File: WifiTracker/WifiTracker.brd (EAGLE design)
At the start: 80 x 44.1 mm, 23 parts, among them Y1 16MHz

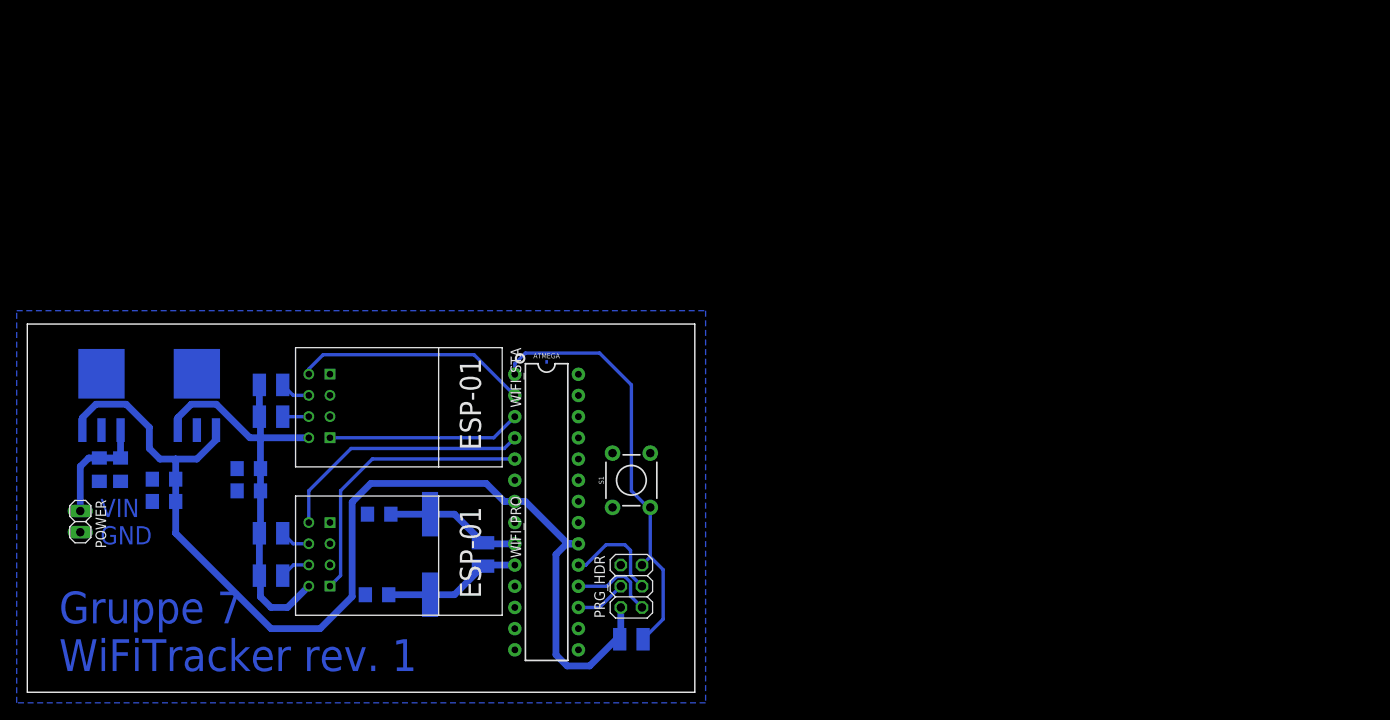
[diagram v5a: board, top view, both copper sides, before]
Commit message: Added 5v to 3.3V regulators to Wifitrackers
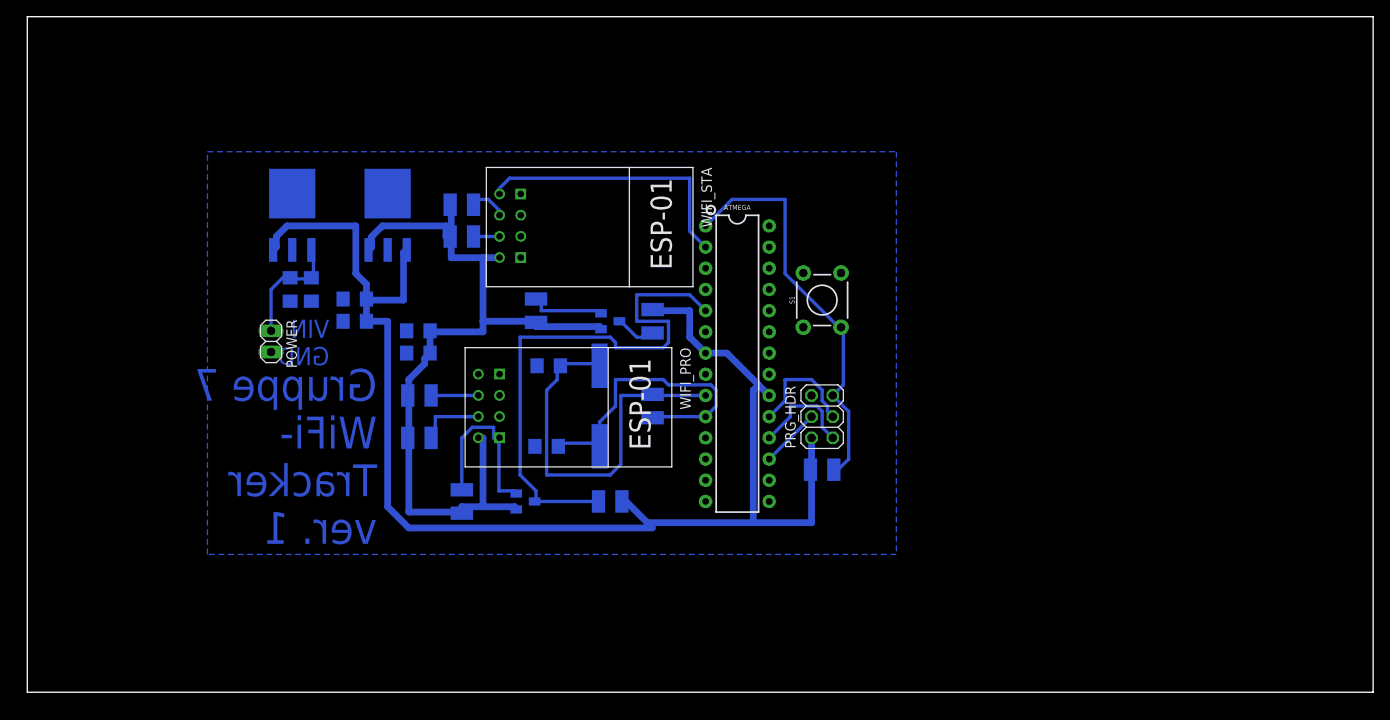
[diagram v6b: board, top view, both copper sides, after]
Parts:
- added Q1, Q2: BSS123, transistor-small-signal:SOT23
- added R10, R7, R8, R9: 10kΩ, eagle-ltspice:R1210
- R1, R2: value 10KOHM -> 10KΩ
- R3, R5, R6: value 10KOHM -> 10kΩ
- R4: value 1MOHM -> 1MΩ
- moved R1 31.4 mm to (52.1, 58.4)
- moved S1 31.4 mm to (95.2, 47.0)
- moved WIFI_STA 31.4 mm to (64.8, 55.9)
- moved C8 31.4 mm to (39.2, 44.5)
- moved 3V_REG 31.4 mm to (43.2, 57.1)
- moved 5V_REG 31.4 mm to (31.8, 57.1)
- moved C4 31.4 mm to (31.5, 48.3)
- moved C5 31.4 mm to (39.2, 47.1)
- moved C7 31.4 mm to (34.0, 48.3)
- moved POWER 31.4 mm to (29.2, 42.0)
- moved R2 31.4 mm to (52.1, 54.6)
- moved PRG_HDR 30.6 mm to (95.2, 33.0)
- moved R6 30.6 mm to (95.2, 26.7)
- moved ATMEGA 29.0 mm to (85.1, 39.4)
- moved C1 27.0 mm to (62.5, 39.1)
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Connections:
- new net N$1: WIFI_PRO.TX
- new net N$2: WIFI_STA.RX
- new net N$3: Q1.2, R7.2, WIFI_PRO.RX
- new net N$4: Q2.2, R9.2
- new net PRO_RXD1: Q2.3, R10.2
- net 3VCC: now also Q1.1, Q2.1, R7.1, R9.1
- net 5VCC: now also R10.1, R8.1
- net GND: no longer WIFI_PRO.GPIO2, WIFI_STA.GPIO2
- net PRO_RXD: now also Q1.3, R8.2; no longer WIFI_PRO.RX
- net PRO_TXD: no longer WIFI_PRO.TX
- net STA_RXD: no longer WIFI_STA.RX
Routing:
- net 3VCC: track 52.5 -> 101.8 mm
- net PRO_RXD: track 34.4 -> 65.8 mm
- net 5VCC: track 131.8 -> 163.2 mm
- net PRO_TXD: track 31.1 -> 0.00 mm
- net XTAL1: track 16.3 -> 46.9 mm
- net STA_RXD: track 23.2 -> 0.00 mm
- net N$3: track 0.00 -> 22.1 mm
- net XTAL2: track 17.0 -> 37.0 mm
- net N$4: track 0.00 -> 10.0 mm
- net PRO_RXD1: track 0.00 -> 5.27 mm
- net STA_TXD: track 28.0 -> 33.1 mm
- net PRO_RST: track 3.65 -> 8.20 mm
- net ATMEGA_RESET: track 52.0 -> 48.6 mm
- net MISO: track 10.6 -> 12.6 mm
- net PRO_CH_PD: track 3.64 -> 5.66 mm
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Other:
- board size 80 x 44.1 mm -> 161.3 x 81 mm
- board text added: "Gruppe 7 WiFi- Tracker ver. 1"
- board text removed: "."
- board text removed: "Gruppe 7 WiFiTracker rev. 1"

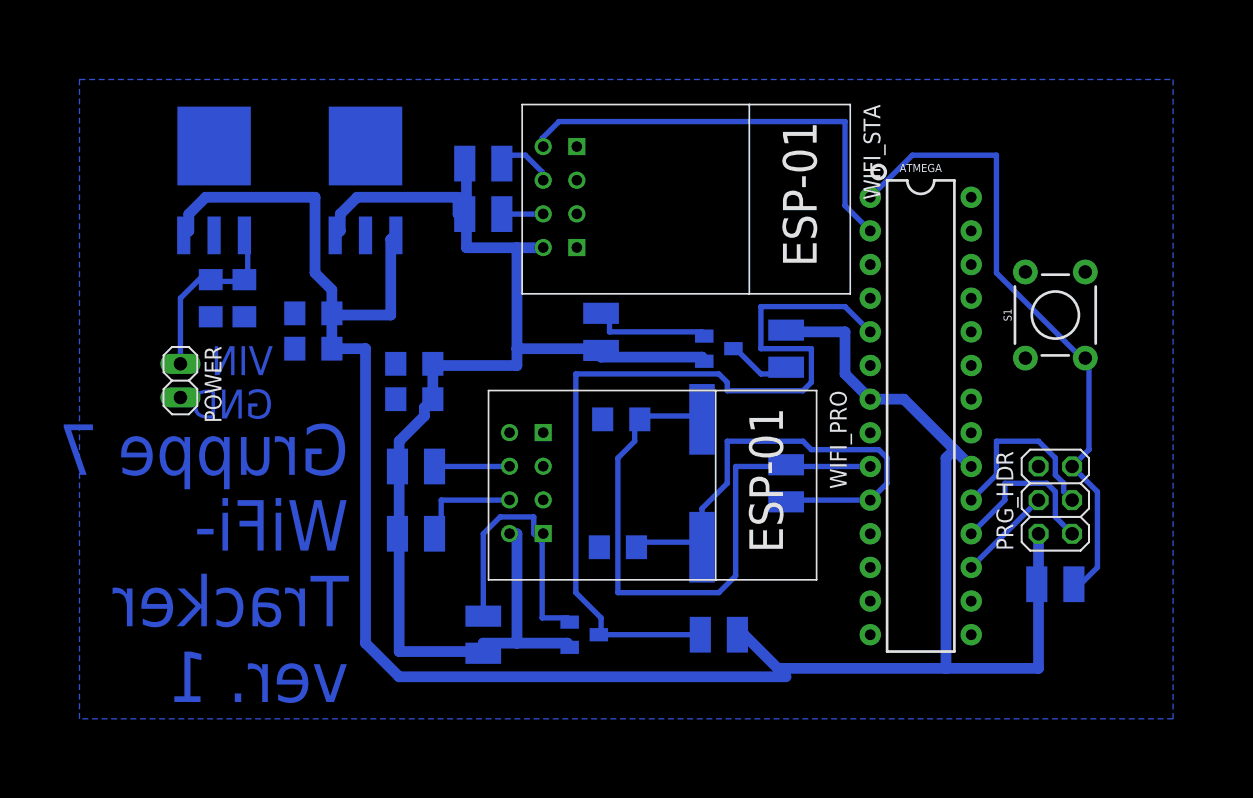
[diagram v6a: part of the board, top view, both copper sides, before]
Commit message: Changed 3.3V regulator
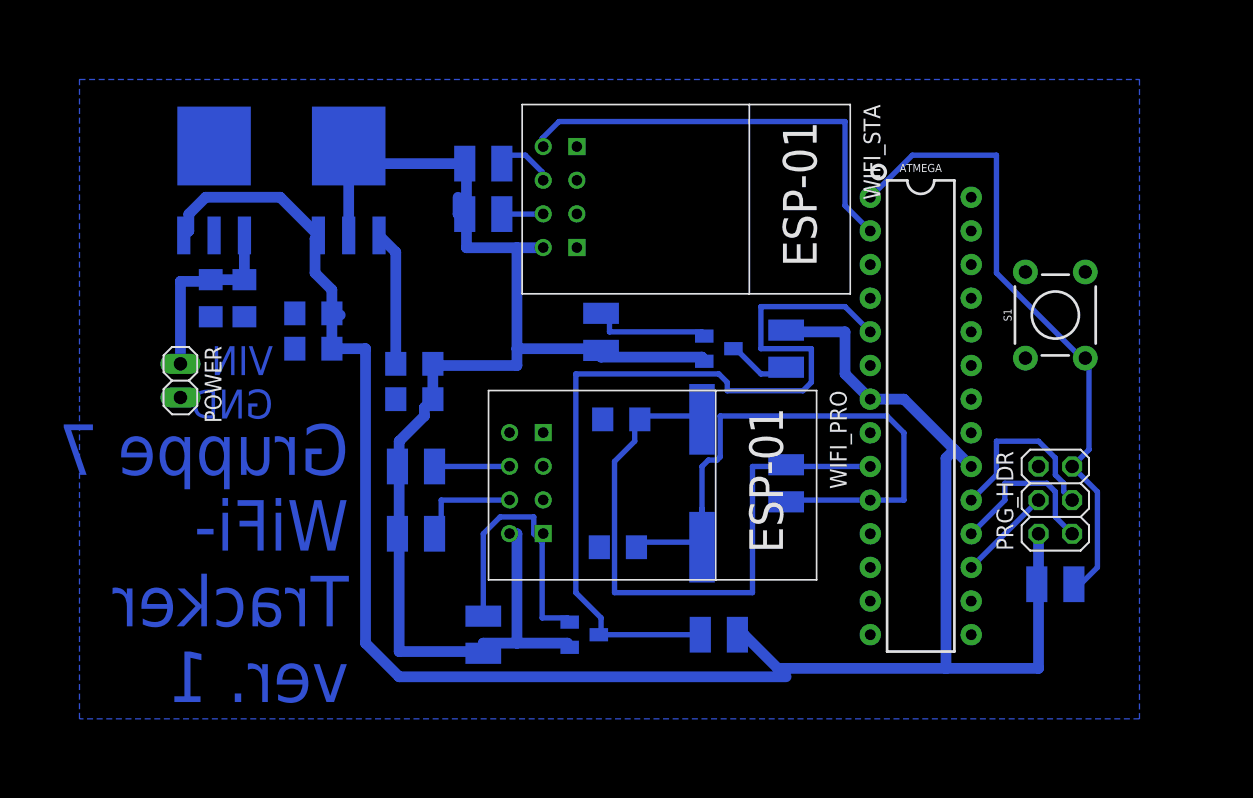
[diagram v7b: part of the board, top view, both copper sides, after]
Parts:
- removed 3V_REG: LP2950CDT-5.0G, LP2950CDT-5.0G:TO229P990X238-4N
- added IC1: TS1117CP33-R0, TS1117CP33-R0:TO229P990X238-4N
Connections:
- net 3VCC: now also IC1.2, IC1.4; no longer 3V_REG.3
- net 5VCC: now also IC1.3; no longer 3V_REG.1
- net GND: now also IC1.1; no longer 3V_REG.2, 3V_REG.4
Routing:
- net 5VCC: track 163.2 -> 151.8 mm
- net XTAL2: track 37.0 -> 47.7 mm
- net GND: track 0.00 -> 10.2 mm
- net 3VCC: track 101.8 -> 106.8 mm
- net XTAL1: track 46.9 -> 48.0 mm
- net VIN: track 14.4 -> 15.3 mm

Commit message: Prepare to print
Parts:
- removed Q1, Q2: BSS123, transistor-small-signal:SOT23
- R10, R8: value 10kΩ -> 2.2kΩ
- R7, R9: value 10kΩ -> 1kΩ
- moved R8 25.0 mm to (57.1, 44.5)
- moved R7 24.4 mm to (63.5, 44.5), turned to 0 degrees
- moved R10 13.7 mm to (64.6, 53.5), turned to 90 degrees
- moved R9 12.0 mm to (71.1, 52.1), turned to 0 degrees
- moved R6 2.54 mm to (95.4, 24.1)
- moved PRG_HDR 2.54 mm to (95.2, 30.5)
- moved S1 0.36 mm to (95.0, 47.2), turned to 270 degrees
- moved C6 0.13 mm to (47.0, 40.6), turned to 180 degrees
- moved C9 0.13 mm to (47.0, 43.3), turned to 180 degrees
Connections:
- removed net N$1: WIFI_PRO.TX
- removed net N$2: WIFI_STA.RX
- removed net N$3: Q1.2, R7.2, WIFI_PRO.RX
- removed net N$4: Q2.2, R9.2
- removed net PRO_RXD1: Q2.3, R10.2
- new net AT_STXD: ATMEGA.5, R7.1
- new net AT_TXD: ATMEGA.3, R9.1
- net 3VCC: no longer Q1.1, Q2.1, R7.1, R9.1
- net 5VCC: no longer R10.1, R8.1
- net GND: now also R10.2, R8.2
- net PRO_RXD: now also R7.2, R8.1, WIFI_PRO.RX; no longer ATMEGA.5, Q1.3, R8.2
- net PRO_TXD: now also WIFI_PRO.TX
- net STA_RXD: now also R10.1, R9.2, WIFI_STA.RX; no longer ATMEGA.3
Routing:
- net PRO_RXD: track 65.8 -> 18.7 mm
- net 3VCC: track 106.8 -> 64.2 mm
- net PRO_TXD: track 0.00 -> 36.3 mm
- net XTAL1: track 48.0 -> 18.9 mm
- net XTAL2: track 47.7 -> 19.1 mm
- net 5VCC: track 151.8 -> 127.9 mm
- net N$3: track 22.1 -> 0.00 mm
- net AT_STXD: track 0.00 -> 16.9 mm
- net STA_RXD: track 0.00 -> 10.6 mm
- net GND: track 10.2 -> 0.00 mm
- net N$4: track 10.0 -> 0.00 mm
- net AT_TXD: track 0.00 -> 9.29 mm
- net PRO_RXD1: track 5.27 -> 0.00 mm
- net STA_TXD: track 33.1 -> 29.6 mm
- net MISO: track 12.6 -> 10.6 mm
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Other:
- board size 161.3 x 81 mm -> 78.7 x 50.5 mm
- board text added: "Gruppe 7"
- board text removed: "Gruppe 7 WiFi- Tracker ver. 1"
